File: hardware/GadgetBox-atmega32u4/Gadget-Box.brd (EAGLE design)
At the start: 93.5 x 53.5 mm, 44 parts, among them U1 MCP73831T-2ACI/OT, U2 AP2112-3.3, U3 ATMEGA32U4-XUAU, U4 ATMEGA32U4-XUMU, X1 CRYSTAL-0500290P1, X100 JSTPH

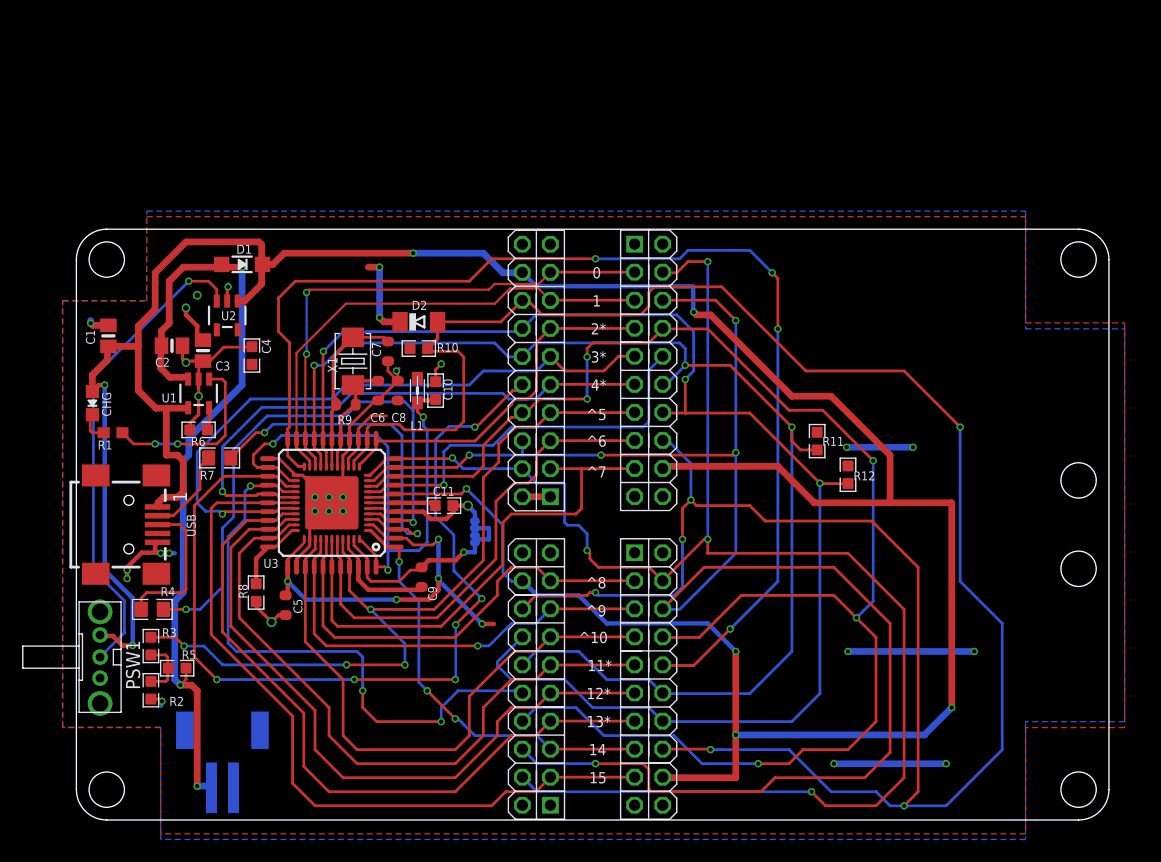
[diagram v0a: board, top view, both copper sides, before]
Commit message: WIP on 32u4
flipping to standard layout
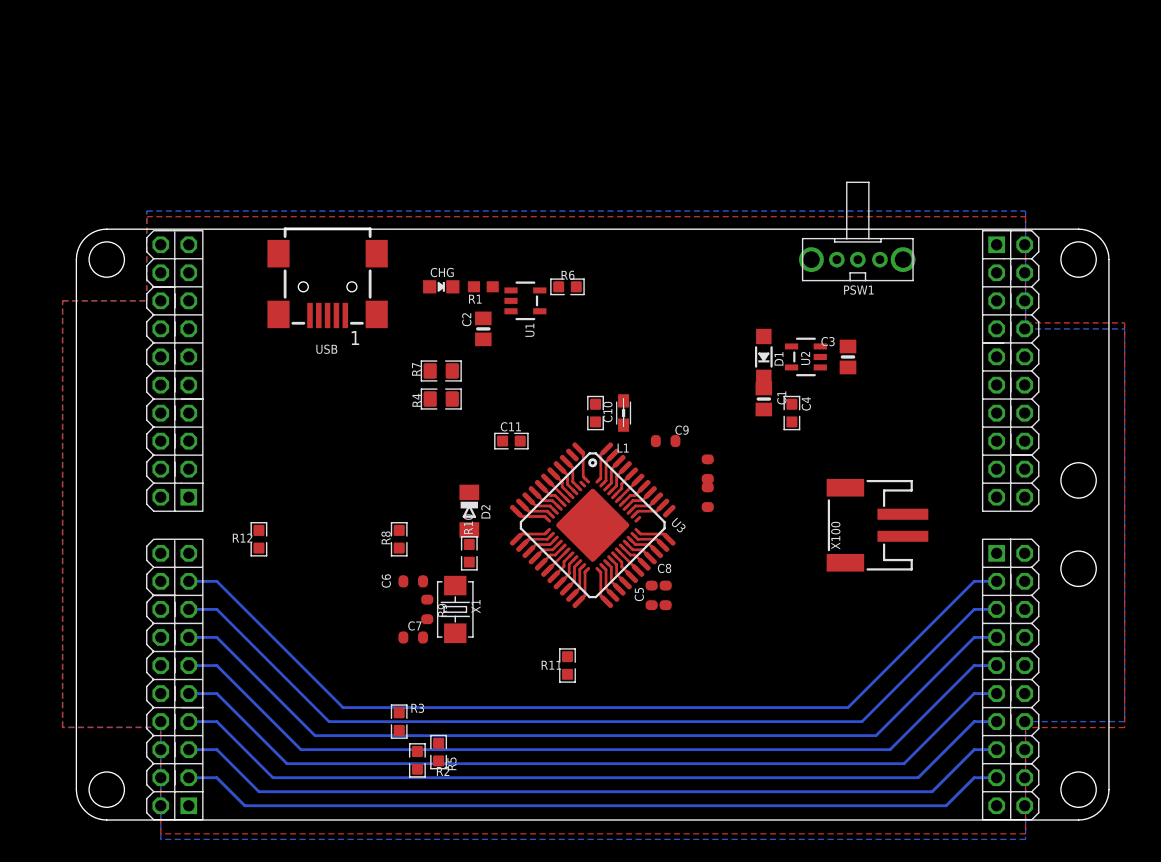
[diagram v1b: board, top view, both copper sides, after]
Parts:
- R100, R101: device SmartPrj:R0402 -> SmartPrj:R0603-ROUND
- moved PSW1 77.5 mm to (72.0, 52.0), turned to 180 degrees
- moved X100 61.3 mm to (72.4, 27.9), flipped to the top, turned to 90 degrees
- moved C1 59.6 mm to (63.5, 39.4), turned to 270 degrees
- moved C3 58.4 mm to (71.1, 43.2), turned to 90 degrees
- moved R12 53.7 mm to (17.8, 26.7), turned to 270 degrees
- moved U2 52.5 mm to (67.3, 43.2), turned to 90 degrees
- moved C4 49.2 mm to (66.0, 38.1)
- moved D1 48.0 mm to (63.5, 43.2), turned to 90 degrees
- moved R1 36.0 mm to (38.1, 49.5)
- moved R6 35.8 mm to (45.7, 49.5), turned to 0 degrees
- moved CHG 33.3 mm to (34.3, 49.5), turned to 270 degrees
- moved C5 33.2 mm to (53.3, 21.6), turned to 90 degrees
- moved AL 32.8 mm to (83.3, 52.1)
- moved AH 32.8 mm to (83.3, 24.1)
- moved BL 32.8 mm to (12.7, 3.81)
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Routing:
- net VBUS: track 281.0 -> 2.65 mm, vias 8 -> 0
- net RESET: track 222.8 -> 3.02 mm, vias 6 -> 0
- net SPI-MOSI: track 146.3 -> 3.02 mm, vias 5 -> 0
- net SPI-MISO: track 143.5 -> 3.15 mm, vias 5 -> 0
- net SPI-SCK: track 141.7 -> 2.90 mm, vias 5 -> 0
- net I2C-SCL: track 128.3 -> 2.65 mm, vias 3 -> 0
- net I2C-SDA: track 113.7 -> 2.77 mm, vias 3 -> 0
- net SPI-CS4: track 105.9 -> 3.15 mm, vias 4 -> 0
- net 3V3: track 84.9 -> 2.90 mm, vias 14 -> 0
- net SPI-CS1: track 83.4 -> 2.90 mm, vias 6 -> 0
- net VBAT: track 73.0 -> 0.00 mm, vias 3 -> 0
- net D5/A5: track 74.5 -> 2.77 mm, vias 4 -> 0
- net GND: track 75.5 -> 8.94 mm, vias 19 -> 0
- net D3*: track 58.5 -> 2.65 mm, vias 1 -> 0
- net SPI-CS2: track 53.7 -> 2.77 mm, vias 3 -> 0
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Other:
- board text removed: "0"
- board text removed: "1"
- board text removed: "11*"
- board text removed: "12*"
- board text removed: "13*"
- board text removed: "14"
- board text removed: "15"
- board text removed: "2*"
- board text removed: "3*"
- board text removed: "4*"
- board text removed: "^10"
- board text removed: "^5"
- board text removed: "^6"
- board text removed: "^7"
- board text removed: "^8"
- board text removed: "^9"

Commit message: more 32u4 progress
50 airwires left
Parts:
- moved C2 46.0 mm to (73.7, 16.5), turned to 0 degrees
- moved CHG 44.2 mm to (68.6, 21.6), turned to 0 degrees
- moved R6 43.3 mm to (78.7, 21.6), turned to 90 degrees
- moved R1 42.3 mm to (73.7, 26.7)
- moved U1 41.5 mm to (73.7, 21.6), turned to 180 degrees
- moved R3 38.1 mm to (61.0, 33.0), turned to 0 degrees
- moved R2 37.4 mm to (61.0, 30.5), turned to 0 degrees
- moved R12 34.2 mm to (50.8, 17.8), turned to 180 degrees
- moved R5 32.4 mm to (61.0, 25.4), turned to 0 degrees
- moved R8 26.9 mm to (55.9, 17.8), turned to 0 degrees
- moved R101 25.3 mm to (34.3, 38.1), turned to 0 degrees
- moved C8 20.5 mm to (34.3, 24.1), turned to 180 degrees
- moved X100 17.8 mm to (73.7, 10.2)
- moved R7 12.0 mm to (45.7, 38.1), turned to 180 degrees
- moved C3 11.7 mm to (78.7, 34.3)
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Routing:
- net VBUS: track 2.65 -> 122.6 mm, vias 0 -> 4
- net D5/A5: track 2.77 -> 87.7 mm
- net D0/RX/MISO: track 2.90 -> 85.1 mm, vias 0 -> 1
- net D3*: track 2.65 -> 84.1 mm, vias 0 -> 1
- net D6/A4: track 2.65 -> 83.2 mm, vias 0 -> 1
- net D7/A3: track 2.53 -> 82.2 mm, vias 0 -> 1
- net D2*: track 3.15 -> 82.6 mm, vias 0 -> 1
- net D1/TX/MISO: track 3.02 -> 82.4 mm, vias 0 -> 1
- net D4*: track 2.65 -> 81.8 mm, vias 0 -> 1
- net VBAT: track 0.00 -> 52.3 mm
- net 3V3: track 2.90 -> 47.4 mm, vias 0 -> 4
- net D-: track 0.00 -> 27.6 mm
- net EN: track 0.00 -> 23.7 mm, vias 0 -> 2
- net D15: track 77.8 -> 99.6 mm, vias 0 -> 3
- net D+: track 0.00 -> 20.7 mm
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- added copper zone on layer 16, net 3V3
- added copper zone on layer 1, net GND
- removed copper zone on layer 1, net 3V3
- removed copper zone on layer 16, net GND

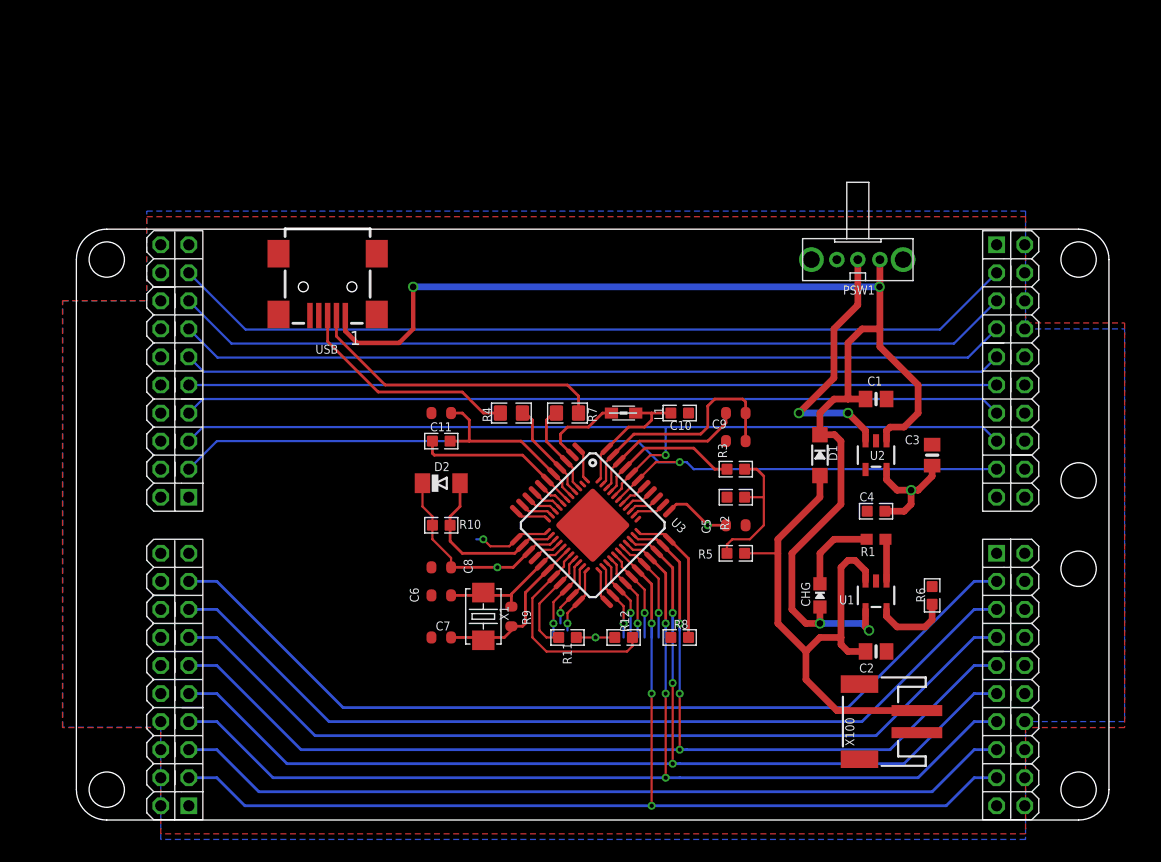
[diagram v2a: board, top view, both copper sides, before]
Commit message: traces done, beeds labels straightened
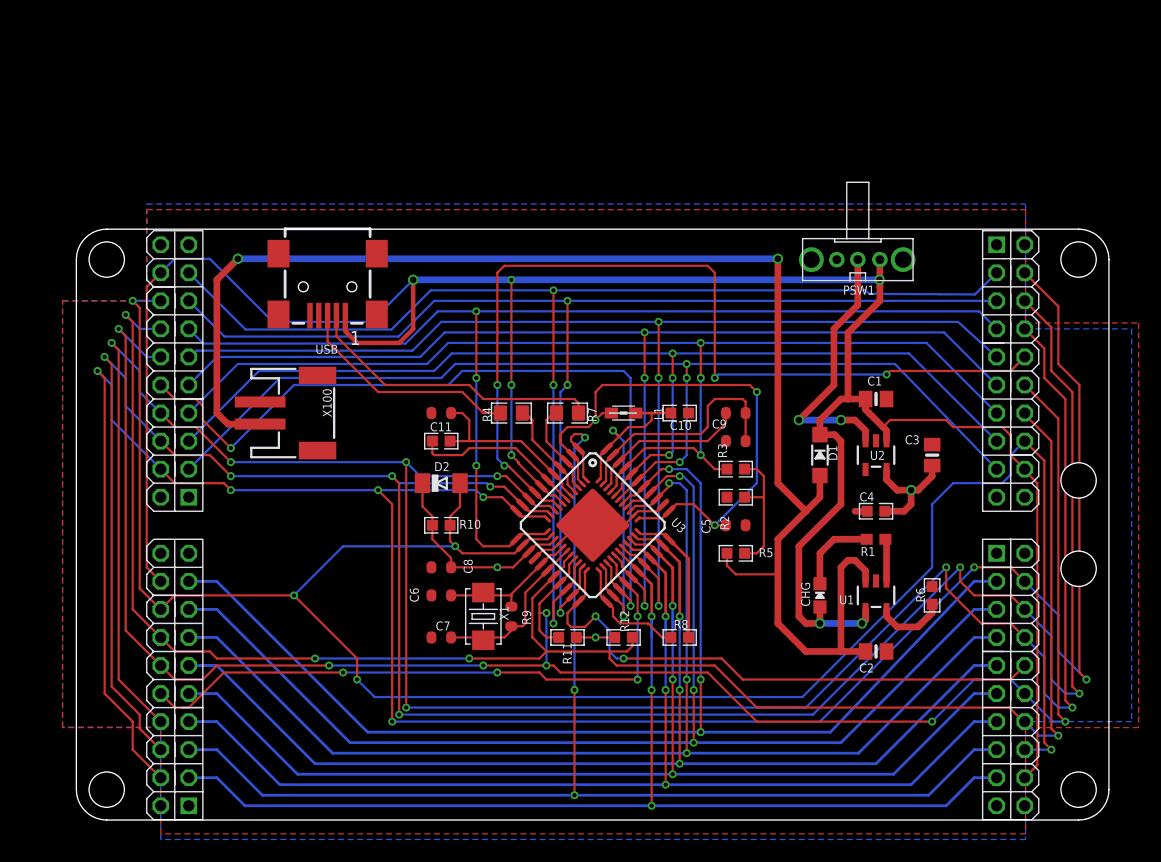
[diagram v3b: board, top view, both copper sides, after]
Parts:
- moved X100 59.1 mm to (21.6, 38.1), turned to 270 degrees
- turned R5 to 180 degrees
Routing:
- net SPI-MISO: track 3.15 -> 222.8 mm, vias 0 -> 7
- net SPI-MOSI: track 3.02 -> 219.9 mm, vias 0 -> 7
- net SPI-SCK: track 2.90 -> 216.0 mm, vias 0 -> 7
- net RESET: track 15.9 -> 192.9 mm, vias 0 -> 5
- net I2C-SDA: track 9.84 -> 172.4 mm, vias 0 -> 7
- net I2C-SCL: track 19.5 -> 164.4 mm, vias 0 -> 4
- net VBUS: track 122.6 -> 232.6 mm, vias 4 -> 7
- net VBAT: track 52.3 -> 133.3 mm, vias 0 -> 2
- net SPI-CS3: track 2.77 -> 82.9 mm, vias 0 -> 4
- net SPI-CS1: track 7.68 -> 74.3 mm, vias 1 -> 2
- net SPI-CS2: track 8.15 -> 57.2 mm, vias 1 -> 4
- net SPI-CS4: track 6.16 -> 51.5 mm, vias 1 -> 2
- net 3V3: track 47.4 -> 84.9 mm, vias 4 -> 6
- net D14: track 79.5 -> 115.3 mm, vias 0 -> 3
- net D8/A2: track 85.3 -> 116.1 mm, vias 0 -> 3
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
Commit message: cleaned up drc
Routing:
- net VBAT: track 133.3 -> 132.4 mm
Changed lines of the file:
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@@
 <wire x1="50.975846875" y1="22.707409375" x2="50.165" y2="23.51825625" width="0.2032" layer="1"/>
 <wire x1="8.89" y1="12.7" x2="10.16" y2="11.43" width="0.2032" layer="1"/>
-<wire x1="10.16" y1="11.43" x2="11.43" y2="11.43" width="0.2032" layer="1"/>
-<wire x1="11.43" y1="11.43" x2="14.605" y2="14.605" width="0.2032" layer="1"/>
-<wire x1="14.605" y1="14.605" x2="25.4" y2="14.605" width="0.2032" layer="1"/>
+<wire x1="10.16" y1="11.43" x2="12.065" y2="11.43" width="0.2032" layer="1"/>
+<wire x1="12.065" y1="11.43" x2="15.24" y2="14.605" width="0.2032" layer="1"/>
+<wire x1="15.24" y1="14.605" x2="25.4" y2="14.605" width="0.2032" layer="1"/>
 <wire x1="39.37" y1="14.605" x2="43.18" y2="14.605" width="0.2032" layer="1"/>
 <wire x1="43.18" y1="14.605" x2="43.815" y2="13.97" width="0.2032" layer="1"/>
@@
 <wire x1="14.97" y1="37.1" x2="13.97" y2="38.1" width="0.6096" layer="1"/>
 <wire x1="13.97" y1="38.1" x2="13.97" y2="50.165" width="0.6096" layer="1"/>
-<wire x1="13.97" y1="50.165" x2="15.875" y2="52.07" width="0.6096" layer="1"/>
-<via x="15.875" y="52.07" extent="1-16" drill="0.6"/>
-<wire x1="15.875" y1="52.07" x2="64.77" y2="52.07" width="0.6096" layer="16"/>
-<via x="64.77" y="52.07" extent="1-16" drill="0.6"/>
-<wire x1="64.77" y1="52.07" x2="64.77" y2="31.75" width="0.6096" layer="1"/>
+<wire x1="13.97" y1="50.165" x2="15.24" y2="51.435" width="0.6096" layer="1"/>
+<via x="15.24" y="51.435" extent="1-16" drill="0.6"/>
+<wire x1="15.24" y1="51.435" x2="64.77" y2="51.435" width="0.6096" layer="16"/>
+<via x="64.77" y="51.435" extent="1-16" drill="0.6"/>
+<wire x1="64.77" y1="51.435" x2="64.77" y2="31.75" width="0.6096" layer="1"/>
 <wire x1="64.77" y1="31.75" x2="67.31" y2="29.21" width="0.6096" layer="1"/>
 <wire x1="60.16" y1="25.4" x2="60.16" y2="24.295" width="0.2032" layer="1"/>

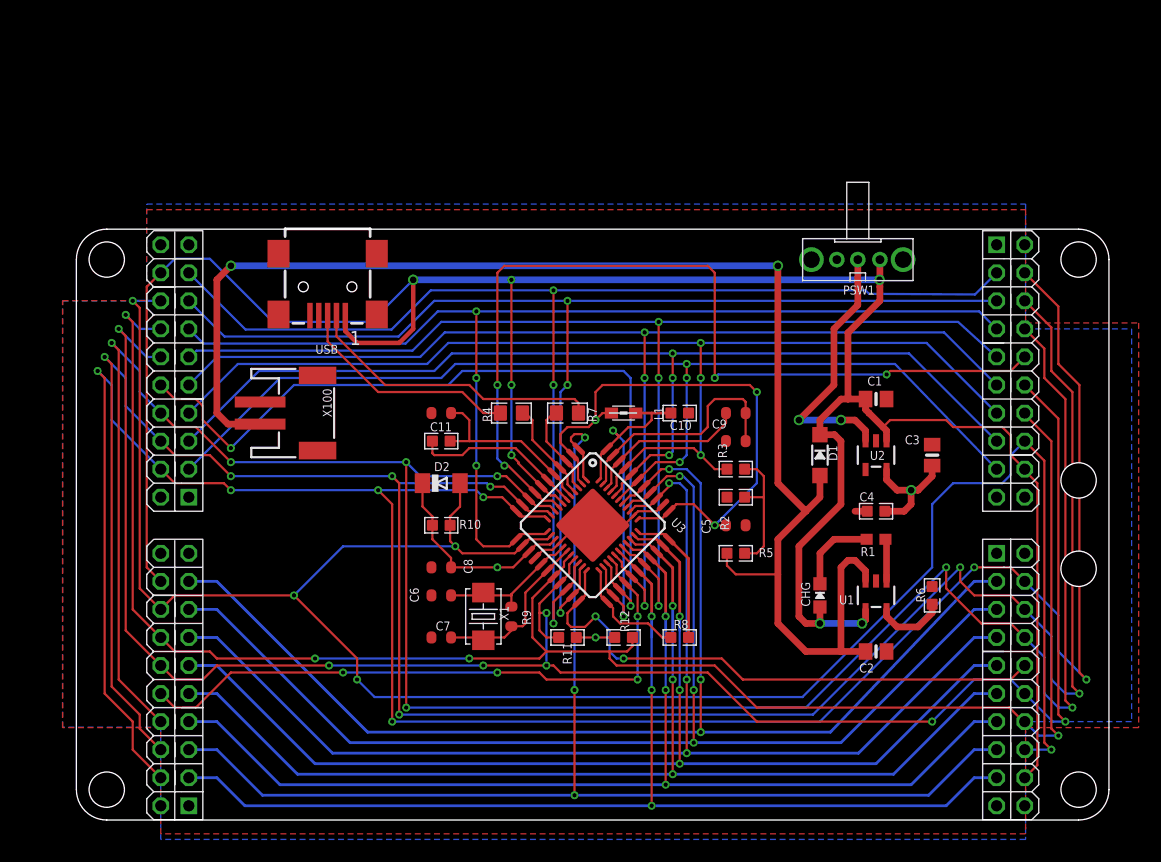
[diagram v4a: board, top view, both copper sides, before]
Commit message: 32u4 V1.8
still needs top silk
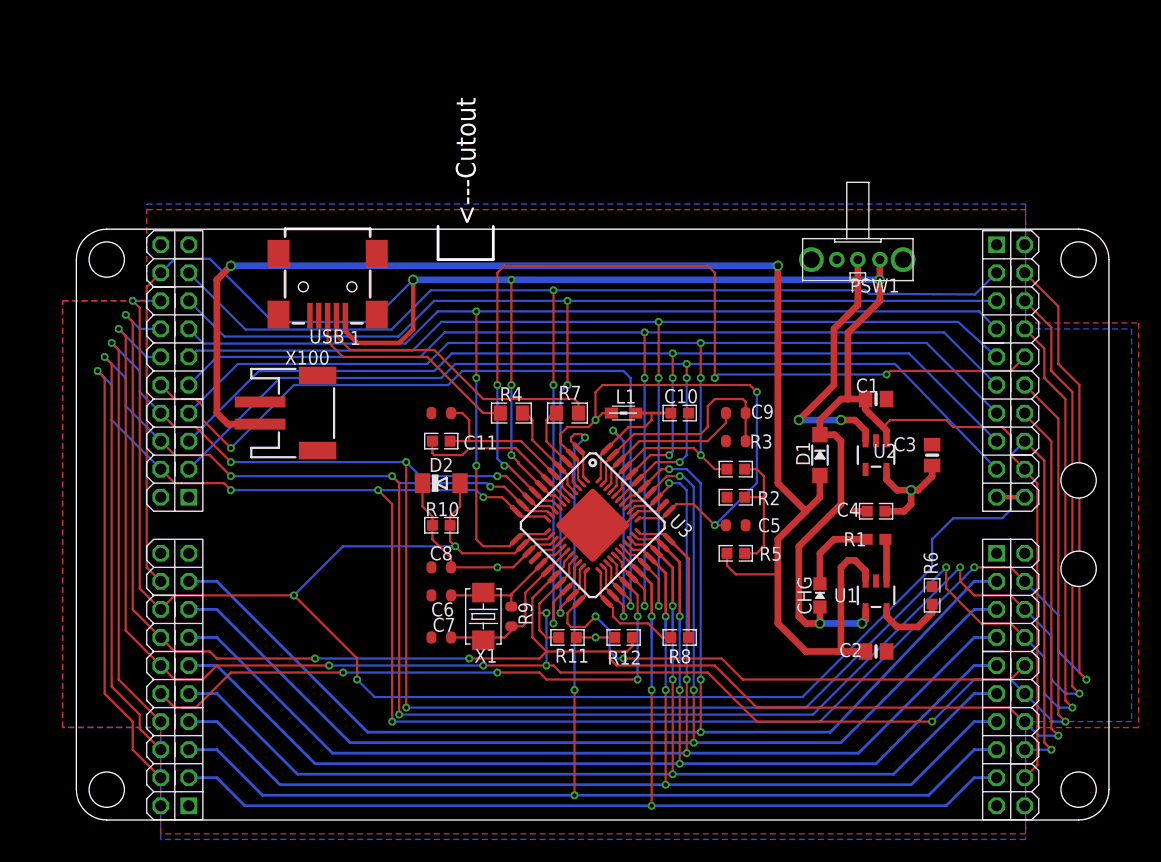
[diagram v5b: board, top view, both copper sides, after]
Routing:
- net 3V3: track 84.9 -> 87.5 mm
- net GND: track 24.0 -> 25.4 mm
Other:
- board text added: "<---Cutout"
- board text added: "Gadget Box Copyright 2016 Gadget Factory, LLC Version 1.8"
- board text removed: "Gadget Box Copyright 2016 Gadget Factory, LLC Version 1.7"
